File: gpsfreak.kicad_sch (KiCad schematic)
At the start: 0 parts

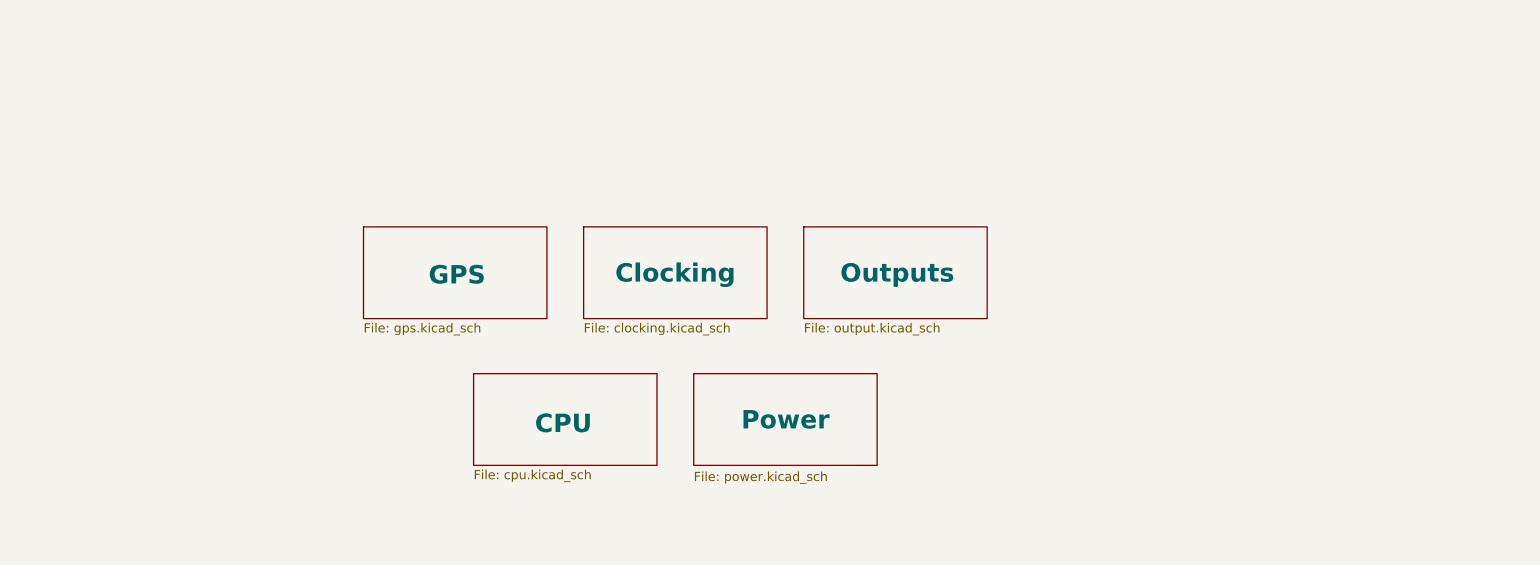
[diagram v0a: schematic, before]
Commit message: Split each output onto it's own sheet.
Makes it easier to mix'n'match output types for board spins.
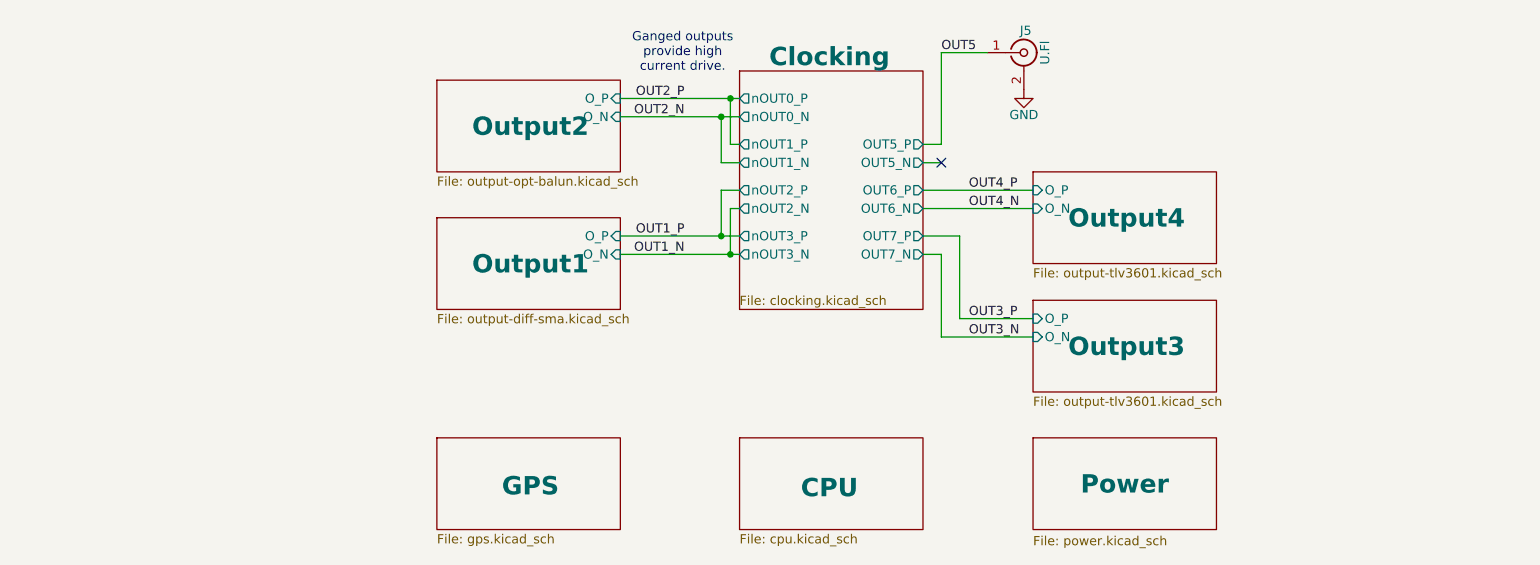
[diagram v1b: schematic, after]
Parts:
- added J5: U.Fl, Parts:U.FL_Hirose_U.FL-R-SMT-1_Vertical, symbol Connector:Conn_Coaxial
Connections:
- new net GND: J5.2 (Ext)
- new net OUT5: J5.1 (In)
- no-connect marks 0 -> 1
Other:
- removed sheet Outputs
- added sheet Output1 (output-diff-sma.kicad_sch)
- added sheet Output2 (output-opt-balun.kicad_sch)
- added sheet Output3 (output-tlv3601.kicad_sch)
- added sheet Output4 (output-tlv3601.kicad_sch)
- sheet Clocking ports: added OUT5_N, OUT5_P, OUT6_N, OUT6_P, OUT7_N, OUT7_P, nOUT0_N, nOUT0_P, nOUT1_N, nOUT1_P, nOUT2_N, nOUT2_P, nOUT3_N, nOUT3_P; removed none
- note added: "Ganged outputs provide high current drive."

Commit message: Touch up net names.
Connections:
- no-connect marks 1 -> 3
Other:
- sheet Clocking ports: added OUT0_N, OUT0_P, OUT1_N, OUT1_P, OUT2_N, OUT2_P, OUT3_N, OUT3_P, OUT4_N, OUT4_P; removed nOUT0_N, nOUT0_P, nOUT1_N, nOUT1_P, nOUT2_N, nOUT2_P, nOUT3_N, nOUT3_P
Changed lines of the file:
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@@
+	)
+	(no_connect
+		(at 179.07 58.42)
 	)
 	(no_connect
 		(at 179.07 67.31)
 	)
-	(wire
-		(pts
-			(xy 179.07 64.77) (xy 179.07 52.07)
+	(no_connect
+		(at 179.07 60.96)
+	)
+	(wire
+		(pts
+			(xy 181.61 64.77) (xy 181.61 52.07)
 		)
 		(stroke
@@
 	(wire
 		(pts
-			(xy 176.53 64.77) (xy 179.07 64.77)
+			(xy 176.53 64.77) (xy 181.61 64.77)
 		)
 		(stroke
@@
 	(wire
 		(pts
-			(xy 179.07 52.07) (xy 185.42 52.07)
+			(xy 176.53 60.96) (xy 179.07 60.96)
+		)
+		(stroke
+			(width 0)
+			(type default)
+		)
+	)
+	(wire
+		(pts
+			(xy 181.61 52.07) (xy 185.42 52.07)
 		)
 		(stroke
@@
 		(pts
 			(xy 134.62 58.42) (xy 149.86 58.42)
+		)
+		(stroke
+			(width 0)
+			(type default)
+		)
+	)
+	(wire
+		(pts
+			(xy 176.53 58.42) (xy 179.07 58.42)
 		)
 		(stroke
@@
 	)
 	(label "OUT5"
-		(at 179.07 52.07 0)
+		(at 181.61 52.07 0)
 		(effects
 			(font
@@
 			)
 		)
-		(pin "nOUT2_N" output
+		(pin "OUT2_N" output
 			(at 151.13 73.66 180)
 			(effects
@@
 			)
 		)
-		(pin "nOUT2_P" output
+		(pin "OUT2_P" output
 			(at 151.13 71.12 180)
 			(effects
@@
 			)
 		)
-		(pin "nOUT3_N" output
+		(pin "OUT3_N" output
 			(at 151.13 80.01 180)
 			(effects
@@
 			)
 		)
-		(pin "nOUT3_P" output
+		(pin "OUT3_P" output
 			(at 151.13 77.47 180)
 			(effects
@@
 			)
 		)
-		(pin "nOUT0_N" output
+		(pin "OUT0_N" output
 			(at 151.13 60.96 180)
 			(effects
@@
 			)
 		)
-		(pin "nOUT0_P" output
+		(pin "OUT0_P" output
 			(at 151.13 58.42 180)
 			(effects
@@
 			)
 		)
-		(pin "nOUT1_N" output
+		(pin "OUT1_N" output
 			(at 151.13 67.31 180)
 			(effects
@@
 			)
 		)
-		(pin "nOUT1_P" output
+		(pin "OUT1_P" output
 			(at 151.13 64.77 180)
 			(effects
@@
 		(pin "OUT5_N" output
 			(at 176.53 67.31 0)
+			(effects
+				(font
+					(size 1.27 1.27)
+				)
+				(justify right)
+			)
+		)
+		(pin "OUT4_N" output
+			(at 176.53 60.96 0)
+			(effects
+				(font
+					(size 1.27 1.27)
+				)
+				(justify right)
+			)
+		)
+		(pin "OUT4_P" output
+			(at 176.53 58.42 0)
 			(effects
 				(font
@@
 			(project "gpsfreak"
 				(path "/3160ff17-81c2-4674-af97-e8d9acaf6b65"
-					(page "2")
+					(page "6")
 				)
 			)
@@
 			(project "gpsfreak"
 				(path "/3160ff17-81c2-4674-af97-e8d9acaf6b65"
-					(page "7")
+					(page "12")
 				)
 			)
@@
 			(project "gpsfreak"
 				(path "/3160ff17-81c2-4674-af97-e8d9acaf6b65"
-					(page "6")
+					(page "11")
 				)
 			)
@@
 			(project "gpsfreak"
 				(path "/3160ff17-81c2-4674-af97-e8d9acaf6b65"
-					(page "1")
+					(page "5")
 				)
 			)
@@
 			(project "gpsfreak"
 				(path "/3160ff17-81c2-4674-af97-e8d9acaf6b65"
-					(page "5")
+					(page "8")
 				)
 			)
@@
 			(project "gpsfreak"
 				(path "/3160ff17-81c2-4674-af97-e8d9acaf6b65"
-					(page "4")
+					(page "7")
 				)
 			)
@@
 			(project "gpsfreak"
 				(path "/3160ff17-81c2-4674-af97-e8d9acaf6b65"
-					(page "8")
+					(page "13")
 				)
 			)
@@
 			(project "gpsfreak"
 				(path "/3160ff17-81c2-4674-af97-e8d9acaf6b65"
-					(page "9")
-				)
-			)
+					(page "14")
+				)
+			)

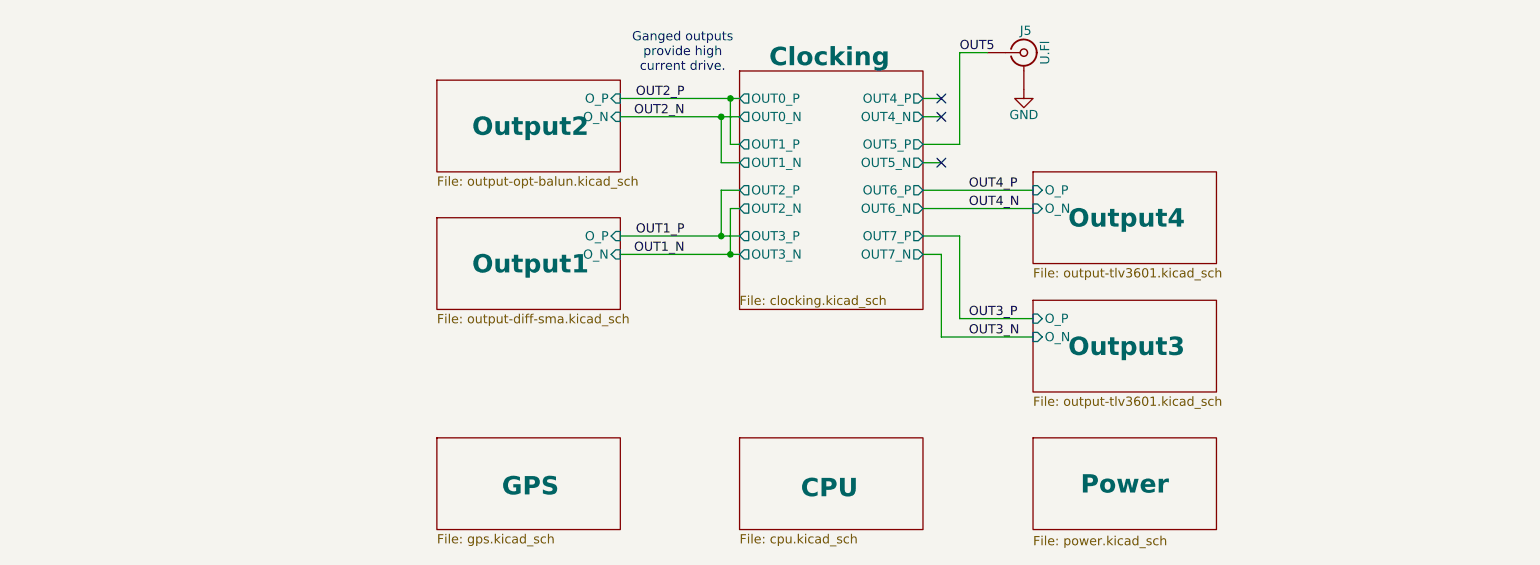
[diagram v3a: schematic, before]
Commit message: FPGA in, layout mostly updated.
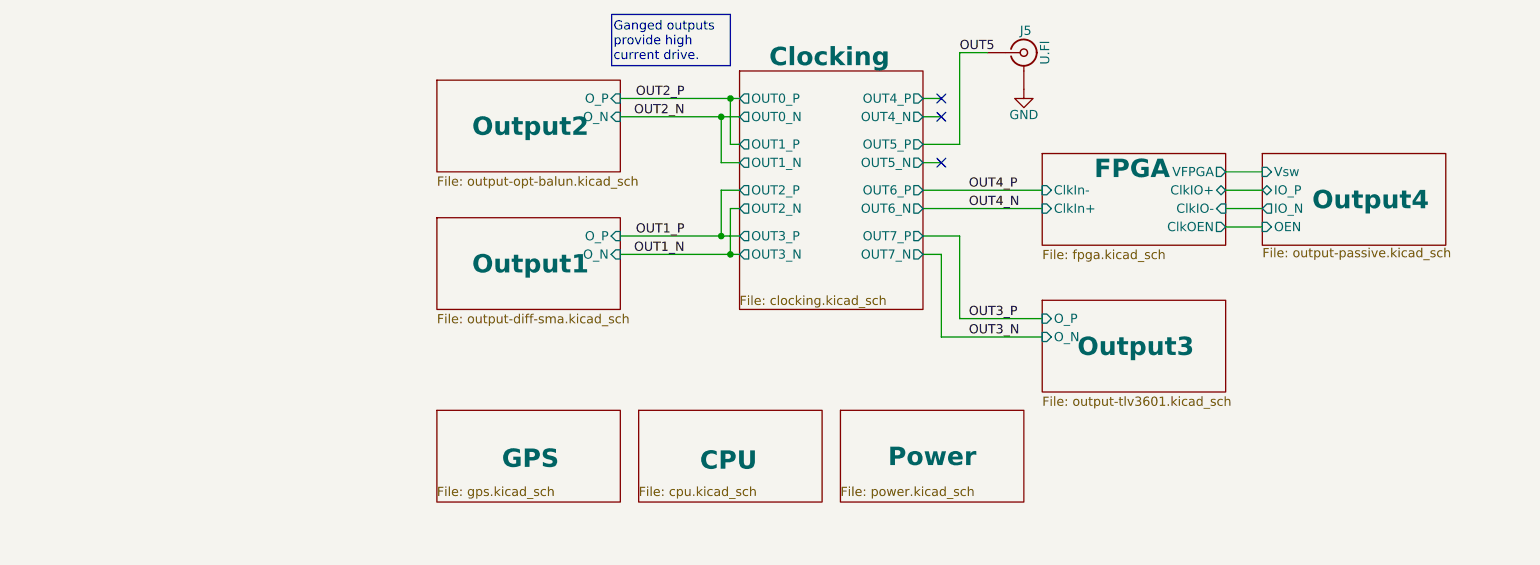
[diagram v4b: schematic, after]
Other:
- added sheet FPGA (fpga.kicad_sch)
- sheet Output4: file output-tlv3601.kicad_sch -> output-passive.kicad_sch
- sheet Output4 ports: added IO_N, IO_P, OEN, Vsw; removed O_N, O_P
- note removed: "Ganged outputs provide high current drive."
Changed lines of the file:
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@@
 	(generator_version "10.0")
 	(paper "A4")
-	(text "Ganged outputs\nprovide high\ncurrent drive.\n"
+	(text_box "Ganged outputs\nprovide high\ncurrent drive.\n"
 		(exclude_from_sim no)
-		(at 143.256 52.07 0)
+		(at 133.4235 46.7812 0)
+		(size 16.4364 7.0851)
+		(margins 0.254 0.254 0.254 0.254)
+		(stroke
+			(width 0)
+			(type default)
+		)
+		(fill
+			(type none)
+		)
 		(effects
 			(font
 				(size 1.27 1.27)
 			)
+			(justify left)
 		)
 	)
@@
 	(wire
 		(pts
-			(xy 181.61 88.9) (xy 191.77 88.9)
+			(xy 181.61 88.9) (xy 193.04 88.9)
 		)
 		(stroke
@@
 	(wire
 		(pts
+			(xy 218.44 76.2) (xy 223.52 76.2)
+		)
+		(stroke
+			(width 0)
+			(type default)
+		)
+	)
+	(wire
+		(pts
 			(xy 148.59 60.96) (xy 148.59 67.31)
 		)
@@
 	(wire
 		(pts
-			(xy 176.53 71.12) (xy 191.77 71.12)
+			(xy 176.53 71.12) (xy 193.04 71.12)
 		)
 		(stroke
@@
 	(wire
 		(pts
+			(xy 218.44 71.12) (xy 223.52 71.12)
+		)
+		(stroke
+			(width 0)
+			(type default)
+		)
+	)
+	(wire
+		(pts
 			(xy 151.13 80.01) (xy 149.86 80.01)
 		)
@@
 	(wire
 		(pts
-			(xy 179.07 91.44) (xy 191.77 91.44)
+			(xy 179.07 91.44) (xy 193.04 91.44)
 		)
 		(stroke
@@
 	(wire
 		(pts
+			(xy 218.44 68.58) (xy 223.52 68.58)
+		)
+		(stroke
+			(width 0)
+			(type default)
+		)
+	)
+	(wire
+		(pts
 			(xy 134.62 77.47) (xy 148.59 77.47)
 		)
@@
 	(wire
 		(pts
-			(xy 176.53 73.66) (xy 191.77 73.66)
+			(xy 176.53 73.66) (xy 193.04 73.66)
+		)
+		(stroke
+			(width 0)
+			(type default)
+		)
+	)
+	(wire
+		(pts
+			(xy 218.44 73.66) (xy 223.52 73.66)
 		)
 		(stroke
@@
 	)
 	(sheet
+		(at 193.04 66.04)
+		(size 25.4 12.7)
+		(exclude_from_sim no)
+		(in_bom yes)
+		(on_board yes)
+		(dnp no)
+		(stroke
+			(width 0.1524)
+			(type solid)
+		)
+		(fill
+			(color 0 0 0 0)
+		)
+		(property "Sheetname" "FPGA"
+			(at 205.486 68.1224 0)
+			(show_name no)
+			(do_not_autoplace no)
+			(effects
+				(font
+					(size 2.54 2.54)
+					(thickness 0.508)
+					(bold yes)
+				)
+			)
+		)
+		(property "Sheetfile" "fpga.kicad_sch"
+			(at 193.04 79.3246 0)
+			(show_name no)
+			(do_not_autoplace no)
+			(effects
+				(font
+					(size 1.27 1.27)
+				)
+				(justify left top)
+			)
+		)
+		(pin "ClkIn+" input
+			(at 193.04 73.66 180)
+			(effects
+				(font
+					(size 1.27 1.27)
+				)
+				(justify left)
+			)
+		)
+		(pin "ClkIn-" input
+			(at 193.04 71.12 180)
+			(effects
+				(font
+					(size 1.27 1.27)
+				)
+				(justify left)
+			)
+		)
+		(pin "ClkIO+" bidirectional
+			(at 218.44 71.12 0)
+			(effects
+				(font
+					(size 1.27 1.27)
+				)
+				(justify right)
+			)
+		)
+		(pin "ClkIO-" input
+			(at 218.44 73.66 0)
+			(effects
+				(font
+					(size 1.27 1.27)
+				)
+				(justify right)
+			)
+		)
+		(pin "ClkOEN" output
+			(at 218.44 76.2 0)
+			(effects
+				(font
+					(size 1.27 1.27)
+				)
+				(justify right)
+			)
+		)
+		(pin "VFPGA" output
+			(at 218.44 68.58 0)
+			(effects
+				(font
+					(size 1.27 1.27)
+				)
+				(justify right)
+			)
+		)
+		(instances
+			(project "gpsfreak"
+				(path "/3160ff17-81c2-4674-af97-e8d9acaf6b65"
+					(page "8")
+				)
+			)
+		)
+	)
+	(sheet
 		(at 109.22 74.93)
 		(size 25.4 12.7)
@@
 	)
 	(sheet
-		(at 109.22 105.41)
+		(at 109.22 101.6)
 		(size 25.4 12.7)
 		(exclude_from_sim no)
@@
 		)
 		(property "Sheetname" "GPS"
-			(at 122.174 112.0644 0)
+			(at 122.174 108.2544 0)
 			(show_name no)
 			(do_not_autoplace no)
@@
 		)
 		(property "Sheetfile" "gps.kicad_sch"
-			(at 109.22 118.6946 0)
-			(show_name no)
-			(do_not_autoplace no)
-			(effects
-				(font
-					(size 1.27 1.27)
-				)
-				(justify left top)
+			(at 109.22 113.6146 0)
+			(show_name no)
+			(do_not_autoplace no)
+			(effects
+				(font
+					(size 1.27 1.27)
+				)
+				(justify left bottom)
 			)
 		)
@@
 	)
 	(sheet
-		(at 191.77 105.41)
+		(at 165.1 101.6)
 		(size 25.4 12.7)
 		(exclude_from_sim no)
@@
 		)
 		(property "Sheetname" "Power"
-			(at 204.47 111.8104 0)
+			(at 177.8 108.0004 0)
 			(show_name no)
 			(do_not_autoplace no)
@@
 		)
 		(property "Sheetfile" "power.kicad_sch"
-			(at 191.77 118.9486 0)
-			(show_name no)
-			(do_not_autoplace no)
-			(effects
-				(font
-					(size 1.27 1.27)
-				)
-				(justify left top)
+			(at 165.1 113.6146 0)
+			(show_name no)
+			(do_not_autoplace no)
+			(effects
+				(font
+					(size 1.27 1.27)
+				)
+				(justify left bottom)
 			)
 		)
@@
 			(project "gpsfreak"
 				(path "/3160ff17-81c2-4674-af97-e8d9acaf6b65"
-					(page "8")
+					(page "9")
 				)
 			)
@@
 	)
 	(sheet
-		(at 151.13 105.41)
+		(at 223.52 66.04)
 		(size 25.4 12.7)
 		(exclude_from_sim no)
@@
 			(color 0 0 0 0)
 		)
-		(property "Sheetname" "CPU"
-			(at 163.576 112.3184 0)
+		(property "Sheetname" "Output4"
+			(at 238.506 72.4404 0)
 			(show_name no)
 			(do_not_autoplace no)
@@
 				(font
 					(size 2.54 2.54)
-					(thickness 0.508)
 					(bold yes)
 				)
 			)
 		)
-		(property "Sheetfile" "cpu.kicad_sch"
-			(at 151.13 118.6946 0)
+		(property "Sheetfile" "output-passive.kicad_sch"
+			(at 223.52 79.0706 0)
 			(show_name no)
 			(do_not_autoplace no)
@@
 				)
 				(justify left top)
+			)
+		)
+		(pin "IO_N" output
+			(at 223.52 73.66 180)
+			(effects
+				(font
+					(size 1.27 1.27)
+				)
+				(justify left)
+			)
+		)
+		(pin "IO_P" bidirectional
+			(at 223.52 71.12 180)
+			(effects
+				(font
+					(size 1.27 1.27)
+				)
+				(justify left)
+			)
+		)
+		(pin "OEN" input
+			(at 223.52 76.2 180)
+			(effects
+				(font
+					(size 1.27 1.27)
+				)
+				(justify left)
+			)
+		)
+		(pin "Vsw" input
+			(at 223.52 68.58 180)
+			(effects
+				(font
+					(size 1.27 1.27)
+				)
+				(justify left)
 			)
 		)
@@
 			(project "gpsfreak"
 				(path "/3160ff17-81c2-4674-af97-e8d9acaf6b65"
-					(page "7")
+					(page "14")
 				)
 			)
@@
 	)
 	(sheet
-		(at 191.77 86.36)
+		(at 137.16 101.6)
 		(size 25.4 12.7)
 		(exclude_from_sim no)
@@
 			(color 0 0 0 0)
 		)
-		(property "Sheetname" "Output3"
-			(at 204.724 92.7604 0)
+		(property "Sheetname" "CPU"
+			(at 149.606 108.5084 0)
 			(show_name no)
 			(do_not_autoplace no)
@@
 			)
 		)
-		(property "Sheetfile" "output-tlv3601.kicad_sch"
-			(at 191.77 99.6446 0)
-			(show_name no)
-			(do_not_autoplace no)
-			(effects
-				(font
-					(size 1.27 1.27)
-				)
-				(justify left top)
-			)
-		)
-		(pin "O_N" input
-			(at 191.77 91.44 180)
-			(effects
-				(font
-					(size 1.27 1.27)
-				)
-				(justify left)
-			)
-		)
-		(pin "O_P" input
-			(at 191.77 88.9 180)
-			(effects
-				(font
-					(size 1.27 1.27)
-				)
-				(justify left)
+		(property "Sheetfile" "cpu.kicad_sch"
+			(at 137.16 113.6146 0)
+			(show_name no)
+			(do_not_autoplace no)
+			(effects
+				(font
+					(size 1.27 1.27)
+				)
+				(justify left bottom)
 			)
 		)
@@
 			(project "gpsfreak"
 				(path "/3160ff17-81c2-4674-af97-e8d9acaf6b65"
-					(page "13")
+					(page "7")
 				)
 			)
@@
 	)
 	(sheet
-		(at 191.77 68.58)
+		(at 193.04 86.36)
 		(size 25.4 12.7)
 		(exclude_from_sim no)
@@
 			(color 0 0 0 0)
 		)
-		(property "Sheetname" "Output4"
-			(at 204.724 74.9804 0)
+		(property "Sheetname" "Output3"
+			(at 205.994 92.7604 0)
 			(show_name no)
 			(do_not_autoplace no)
@@
 		)
 		(property "Sheetfile" "output-tlv3601.kicad_sch"
-			(at 191.77 81.8646 0)
+			(at 193.04 99.6446 0)
 			(show_name no)
 			(do_not_autoplace no)
@@
 		)
 		(pin "O_N" input
-			(at 191.77 73.66 180)
+			(at 193.04 91.44 180)
 			(effects
 				(font
@@
 		)
 		(pin "O_P" input
-			(at 191.77 71.12 180)
+			(at 193.04 88.9 180)
 			(effects
 				(font
@@
 			(project "gpsfreak"
 				(path "/3160ff17-81c2-4674-af97-e8d9acaf6b65"
-					(page "14")
-				)
-			)
+					(page "13")
+				)
+			)

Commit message: Layout down
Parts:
- J5: Stock (none) -> 6
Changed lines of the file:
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@@
+			)
+		)
+		(property "Stock" "6"
+			(at 190.5 52.07 0)
+			(hide yes)
+			(show_name no)
+			(do_not_autoplace no)
+			(effects
+				(font
+					(size 1.27 1.27)
+				)
 			)
 		)
